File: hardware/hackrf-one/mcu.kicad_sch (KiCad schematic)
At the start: 130 parts, among them J11 Connector_USB_C_Receptacle_US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, P1 1V8, P20 GPIO, P22 I2S, P23 DBGEN, P24 TRST, P25 LPC_ISP, P26 LPC_JTAG, P28 SD, P29 CPLD_JTAG, P3 GND, P30 BANK2_AUX, P5 LEDS, P68 SPIFI_CS, P69 VREGMODE, P70 EN_1V8, P72 GP_CLKIN, P73 P1_2, P74 P1_1, P75 GP_CLKIN, P76 GP_CLKIN, P77 GP_CLKIN, P78 GP_CLKIN, P79 GP_CLKIN, P8 VCC, P80 SHIELD, P81 SPIFI_SIO2, P82 SPIFI_SIO3, Q5 BSS84, SW1 DFU, SW2 RESET, U20 W25Q80, U21 TPS62410, U23 LPC4320FBD144, U24 GSG-XC2C64A-7VQG100C, X2 MCU_XTAL, X3 RTC_XTAL

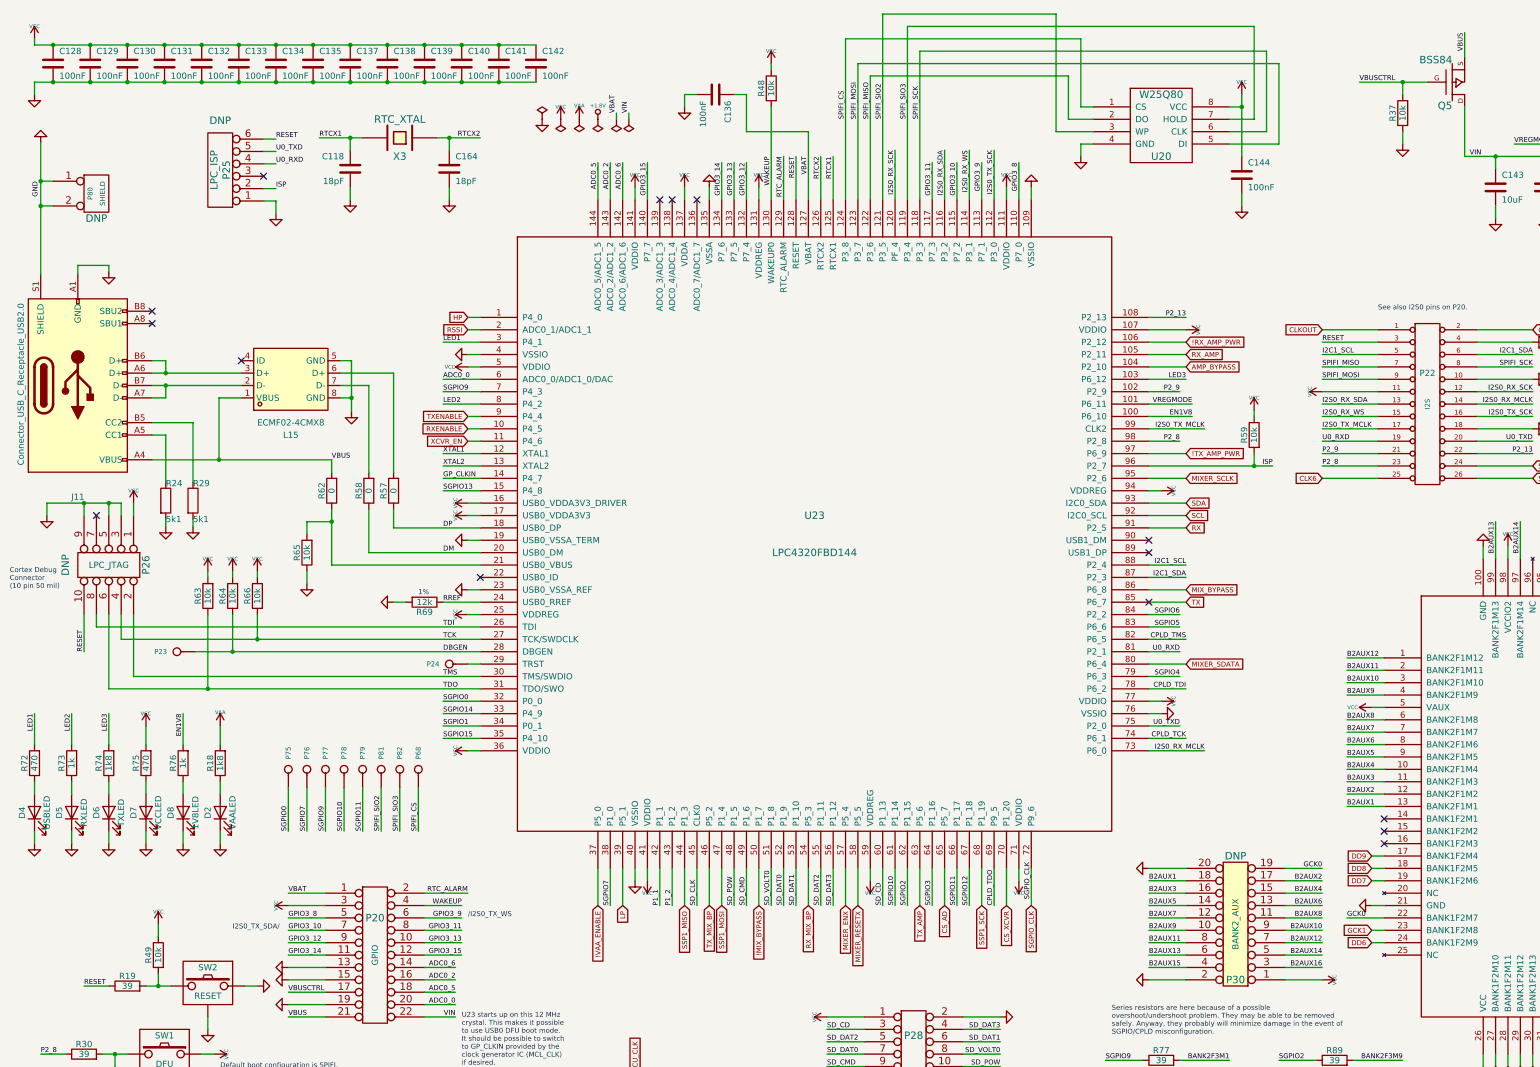
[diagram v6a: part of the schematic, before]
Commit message: Made design changes to indicate version 15. Correct Q3/4/5 part-no and LPF rotation
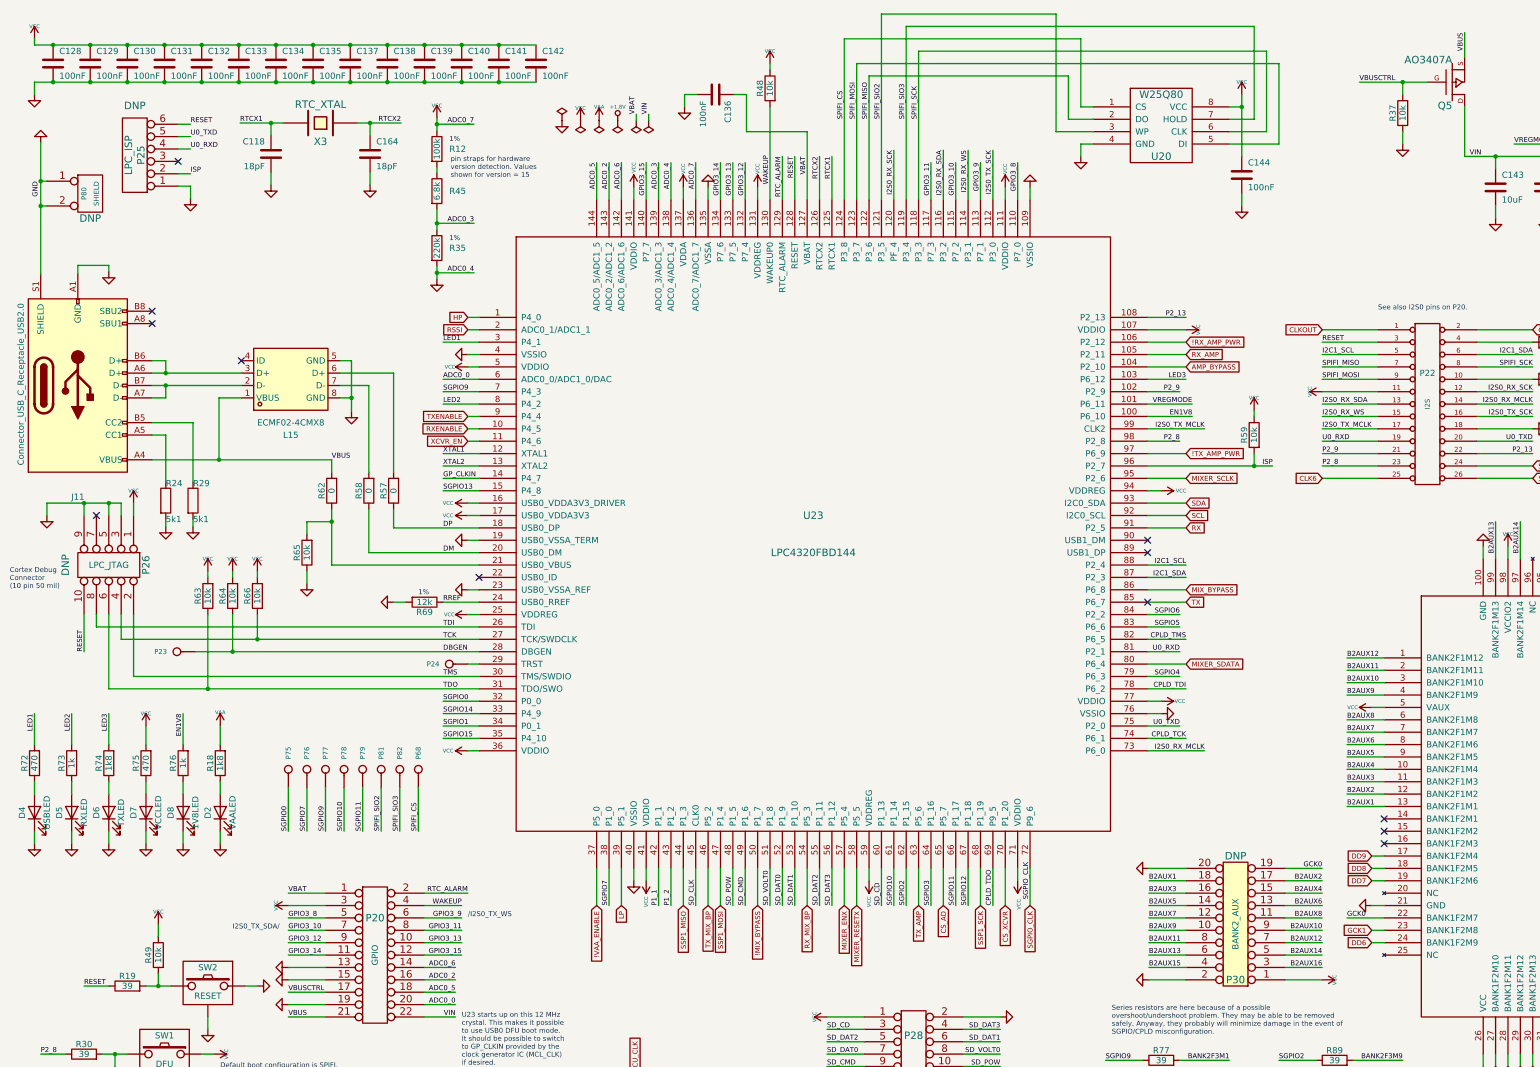
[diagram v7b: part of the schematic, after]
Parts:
- added R12: 100k, hackrf:GSG-0402, symbol Device:R
- added R35: 220k, hackrf:GSG-0402, symbol Device:R
- added R45: 6.8k, hackrf:GSG-0402, symbol Device:R
- Q5: value BSS84 -> AO3407A
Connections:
- net GND: now also U23.138 (ADC0_4/ADC1_4), R35.2
- net VCC: now also U23.136 (ADC0_7/ADC1_7), R12.1
- net ADC0_3: now reaches U23.139 (ADC0_3/ADC1_3)
- net ADC0_3: now also R35.1, R45.2
- new net: R12.2, R45.1
- no-connect marks 22 -> 19
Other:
- note added: "pin straps for hardware version detection. Values shown for version = 15"
- moved on the sheet: C118, C164, P25, P80, X3

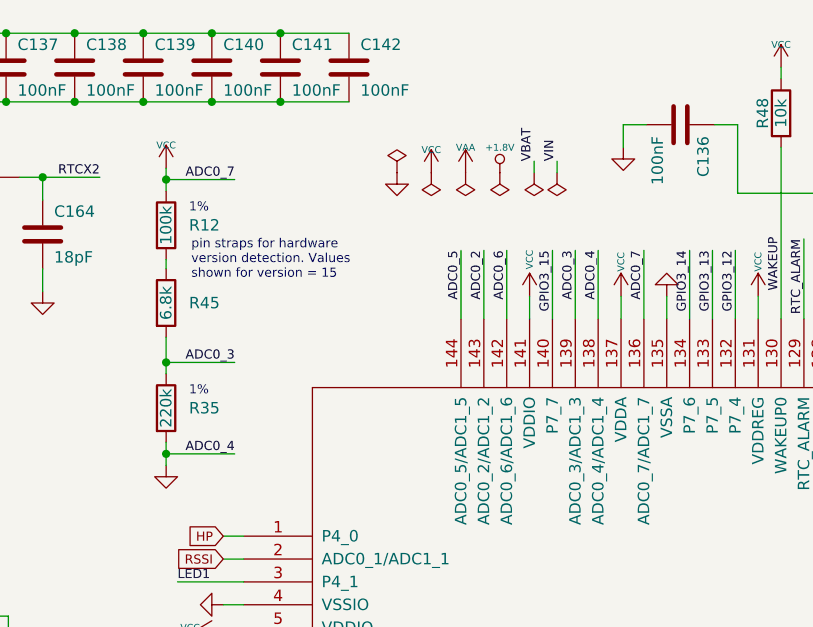
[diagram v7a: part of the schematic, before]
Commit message: Added U15 version detection resistors, corrected FETs and U3 rotation
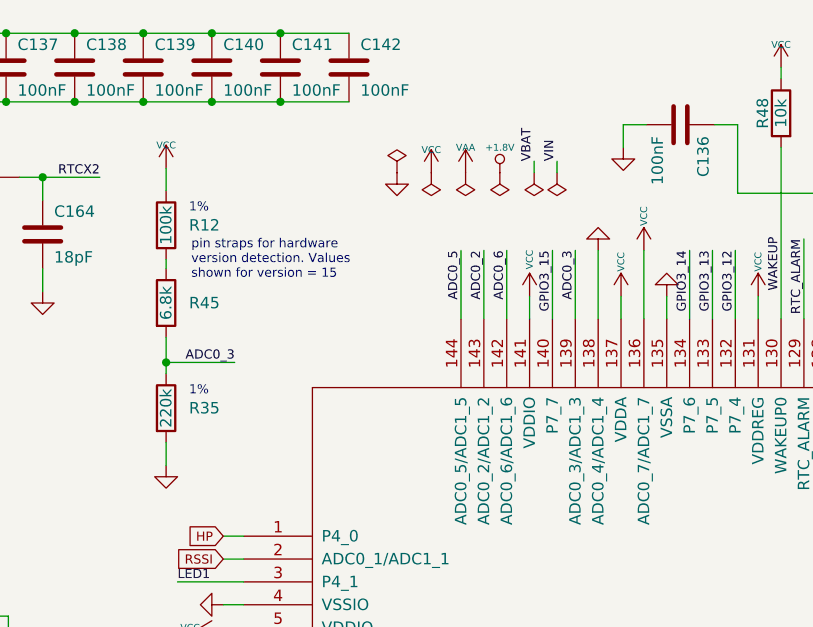
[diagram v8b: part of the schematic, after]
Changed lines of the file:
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@@
 	)
 	(junction
-		(at 100.33 67.056)
-		(diameter 0)
-		(color 0 0 0 0)
-	)
-	(junction
 		(at 53.34 152.4)
 		(diameter 0)
@@
 	)
 	(junction
-		(at 100.33 36.576)
-		(diameter 0)
-		(color 0 0 0 0)
-	)
-	(junction
 		(at 298.45 27.94)
 		(diameter 0)
@@
 	(wire
 		(pts
-			(xy 100.33 67.056) (xy 100.33 68.326)
+			(xy 100.33 65.786) (xy 100.33 68.326)
 		)
 		(stroke
@@
 	(wire
 		(pts
-			(xy 107.95 67.056) (xy 100.33 67.056)
-		)
-		(stroke
-			(width 0)
-			(type default)
-		)
-	)
-	(wire
-		(pts
 			(xy 100.33 45.466) (xy 100.33 46.482)
 		)
@@
 	(wire
 		(pts
-			(xy 100.33 36.576) (xy 100.33 37.846)
+			(xy 100.33 35.306) (xy 100.33 37.846)
 		)
 		(stroke
@@
 	(wire
 		(pts
-			(xy 107.95 36.576) (xy 100.33 36.576)
-		)
-		(stroke
-			(width 0)
-			(type default)
-		)
-	)
-	(wire
-		(pts
 			(xy 353.06 227.33) (xy 353.06 229.87)
 		)
@@
 	(wire
 		(pts
-			(xy 100.33 67.056) (xy 100.33 65.786)
-		)
-		(stroke
-			(width 0)
-			(type default)
-		)
-	)
-	(wire
-		(pts
 			(xy 246.38 196.85) (xy 254 196.85)
 		)
@@
 	(wire
 		(pts
-			(xy 100.33 35.306) (xy 100.33 36.576)
-		)
-		(stroke
-			(width 0)
-			(type default)
-		)
-	)
-	(wire
-		(pts
 			(xy 294.64 204.47) (xy 292.1 204.47)
 		)
@@
 		)
 	)
-	(label "ADC0_7"
-		(at 107.95 36.576 180)
-		(fields_autoplaced yes)
-		(effects
-			(font
-				(size 1.016 1.016)
-			)
-			(justify right bottom)
-		)
-	)
 	(label "U0_RXD"
 		(at 281.94 101.6 0)
@@
 		)
 	)
-	(label "ADC0_7"
-		(at 153.416 44.45 270)
-		(fields_autoplaced yes)
-		(effects
-			(font
-				(size 1.016 1.016)
-			)
-			(justify right bottom)
-		)
-	)
 	(label "B2AUX6"
 		(at 287.02 163.83 0)
@@
 		)
 	)
-	(label "ADC0_4"
-		(at 107.95 67.056 180)
-		(fields_autoplaced yes)
-		(effects
-			(font
-				(size 1.016 1.016)
-			)
-			(justify right bottom)
-		)
-	)
 	(label "SGPIO3"
 		(at 273.05 233.68 0)
@@
 		)
 	)
-	(label "ADC0_4"
-		(at 148.336 44.45 270)
-		(fields_autoplaced yes)
-		(effects
-			(font
-				(size 1.016 1.016)
-			)
-			(justify right bottom)
-		)
-	)
 	(label "CPLD_TCK"
 		(at 370.84 234.95 90)
@@
 	)
 	(symbol
+		(lib_id "hackrf-one:GND-power")
+		(at 148.336 44.45 180)
+		(unit 1)
+		(exclude_from_sim no)
+		(in_bom yes)
+		(on_board yes)
+		(dnp no)
+		(property "Reference" "#PWR057"
+			(at 148.336 44.45 0)
+			(effects
+				(font
+					(size 0.762 0.762)
+				)
+				(hide yes)
+			)
+		)
+		(property "Value" "GND"
+			(at 148.336 42.672 0)
+			(effects
+				(font
+					(size 0.762 0.762)
+				)
+				(hide yes)
+			)
+		)
+		(property "Footprint" ""
+			(at 148.336 44.45 0)
+			(effects
+				(font
+					(size 1.524 1.524)
+				)
+				(hide yes)
+			)
+		)
+		(property "Datasheet" ""
+			(at 148.336 44.45 0)
+			(effects
+				(font
+					(size 1.524 1.524)
+				)
+				(hide yes)
+			)
+		)
+		(property "Description" ""
+			(at 148.336 44.45 0)
+			(effects
+				(font
+					(size 1.27 1.27)
+				)
+				(hide yes)
+			)
+		)
+		(pin "1"
+		)
+		(instances
+			(project "hackrf-one"
+				(path "/00e5afbc-cf8c-40e8-b378-e4fd9cf88403/00000000-0000-0000-0000-00005037043e"
+					(reference "#PWR057")
+					(unit 1)
+				)
+			)
+		)
+	)
+	(symbol
 		(lib_id "hackrf-one:VCC-power")
 		(at 100.33 35.306 0)
@@
 					(unit 1)
 				)
+			)
+		)
+	)
+	(symbol
+		(lib_id "hackrf-one:VCC-power")
+		(at 153.416 44.45 0)
+		(unit 1)
+		(exclude_from_sim no)
+		(in_bom yes)
+		(on_board yes)
+		(dnp no)
+		(property "Reference" "#PWR077"
+			(at 153.416 41.91 0)
+			(effects
+				(font
+					(size 0.762 0.762)
+				)
+				(hide yes)
+			)
+		)
+		(property "Value" "VCC"
+			(at 153.416 40.64 90)
+			(effects
+				(font
+					(size 0.762 0.762)
+				)
+			)
+		)
+		(property "Footprint" ""
+			(at 153.416 44.45 0)
+			(effects
+				(font
+					(size 1.524 1.524)
+				)
+				(hide yes)
+			)
+		)
+		(property "Datasheet" ""
+			(at 153.416 44.45 0)
+			(effects
+				(font
+					(size 1.524 1.524)
+				)
+				(hide yes)
+			)
+		)
+		(property "Description" ""
+			(at 153.416 44.45 0)
+			(effects
+				(font
+					(size 1.27 1.27)
+				)
+				(hide yes)
+			)
+		)
+		(pin "1"
+		)
+		(instances
+			(project "hackrf-one"
+				(path "/00e5afbc-cf8c-40e8-b378-e4fd9cf88403/00000000-0000-0000-0000-00005037043e"
+					(reference "#PWR077")
+					(unit 1)
+				)
